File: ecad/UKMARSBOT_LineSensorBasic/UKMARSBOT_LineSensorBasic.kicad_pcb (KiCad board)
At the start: 2 copper layers, 40.5 x 81.4 mm, 32 parts, among them J1 Conn_01x16, Q1 BC337, Q2 BPW85C, Q3 BPW85C, Q4 BPW85C, Q5 BPW85C, Q6 BC337

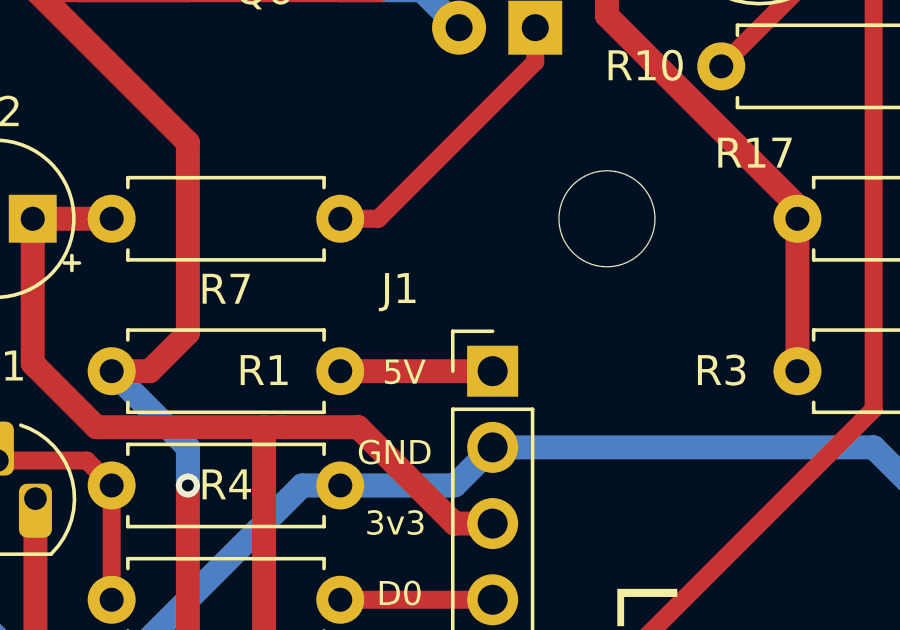
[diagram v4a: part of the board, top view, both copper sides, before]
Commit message: Reworked chassis board for production
Board reworked based on known issues from prototype builds.
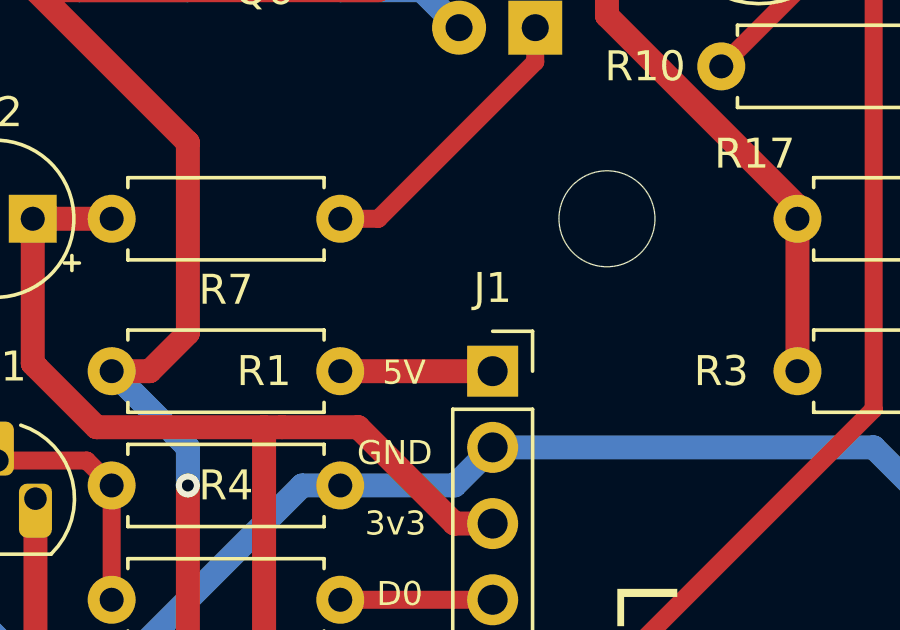
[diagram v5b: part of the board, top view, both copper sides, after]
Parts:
- J1: footprint Connector_PinHeader_2.54mm:PinHeader_1x16_P2.54mm_Vertical -> Connector_PinSocket_2.54mm:PinSocket_1x16_P2.54mm_Vertical
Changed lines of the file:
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@@
 		)
 	)
-	(footprint "Connector_PinHeader_2.54mm:PinHeader_1x16_P2.54mm_Vertical"
+	(footprint "Connector_PinSocket_2.54mm:PinSocket_1x16_P2.54mm_Vertical"
 		(locked yes)
 		(layer "F.Cu")
 		(at 157.48 82.55)
-		(descr "Through hole straight pin header, 1x16, 2.54mm pitch, single row")
-		(tags "Through hole pin header THT 1x16 2.54mm single row")
+		(descr "Through hole straight socket strip, 1x16, 2.54mm pitch, single row (from Kicad 4.0.7), script generated")
+		(tags "Through hole socket strip THT 1x16 2.54mm single row")
 		(property "Reference" "J1"
-			(at -3.084319 -2.733641 0)
+			(at 0 -2.77 0)
 			(layer "F.SilkS")
 			(effects
@@
 		)
 		(property "Value" "Conn_01x16"
-			(at 0 40.43 0)
+			(at 0 40.87 0)
 			(layer "F.Fab")
 			(effects
@@
 			)
 		)
-		(property "Footprint" "Connector_PinHeader_2.54mm:PinHeader_1x16_P2.54mm_Vertical"
+		(property "Footprint" "Connector_PinSocket_2.54mm:PinSocket_1x16_P2.54mm_Vertical"
 			(at 0 0 0)
 			(unlocked yes)
@@
 		(attr through_hole)
 		(fp_line
-			(start -1.33 -1.33)
-			(end 0 -1.33)
-			(stroke
-				(width 0.12)
-				(type solid)
-			)
-			(layer "F.SilkS")
-		)
-		(fp_line
-			(start -1.33 0)
-			(end -1.33 -1.33)
-			(stroke
-				(width 0.12)
-				(type solid)
-			)
-			(layer "F.SilkS")
-		)
-		(fp_line
 			(start -1.33 1.27)
 			(end -1.33 39.43)
@@
 		)
 		(fp_line
+			(start 0 -1.33)
+			(end 1.33 -1.33)
+			(stroke
+				(width 0.12)
+				(type solid)
+			)
+			(layer "F.SilkS")
+		)
+		(fp_line
+			(start 1.33 -1.33)
+			(end 1.33 0)
+			(stroke
+				(width 0.12)
+				(type solid)
+			)
+			(layer "F.SilkS")
+		)
+		(fp_line
 			(start 1.33 1.27)
 			(end 1.33 39.43)
@@
 		(fp_line
 			(start -1.8 -1.8)
+			(end 1.75 -1.8)
+			(stroke
+				(width 0.05)
+				(type solid)
+			)
+			(layer "F.CrtYd")
+		)
+		(fp_line
+			(start -1.8 39.9)
+			(end -1.8 -1.8)
+			(stroke
+				(width 0.05)
+				(type solid)
+			)
+			(layer "F.CrtYd")
+		)
+		(fp_line
+			(start 1.75 -1.8)
+			(end 1.75 39.9)
+			(stroke
+				(width 0.05)
+				(type solid)
+			)
+			(layer "F.CrtYd")
+		)
+		(fp_line
+			(start 1.75 39.9)
 			(end -1.8 39.9)
 			(stroke
@@
 		)
 		(fp_line
-			(start -1.8 39.9)
-			(end 1.8 39.9)
-			(stroke
-				(width 0.05)
-				(type solid)
-			)
-			(layer "F.CrtYd")
-		)
-		(fp_line
-			(start 1.8 -1.8)
-			(end -1.8 -1.8)
-			(stroke
-				(width 0.05)
-				(type solid)
-			)
-			(layer "F.CrtYd")
-		)
-		(fp_line
-			(start 1.8 39.9)
-			(end 1.8 -1.8)
-			(stroke
-				(width 0.05)
-				(type solid)
-			)
-			(layer "F.CrtYd")
-		)
-		(fp_line
-			(start -1.27 -0.635)
-			(end -0.635 -1.27)
+			(start -1.27 -1.27)
+			(end 0.635 -1.27)
 			(stroke
 				(width 0.1)
@@
 		(fp_line
 			(start -1.27 39.37)
-			(end -1.27 -0.635)
-			(stroke
-				(width 0.1)
-				(type solid)
-			)
-			(layer "F.Fab")
-		)
-		(fp_line
-			(start -0.635 -1.27)
-			(end 1.27 -1.27)
-			(stroke
-				(width 0.1)
-				(type solid)
-			)
-			(layer "F.Fab")
-		)
-		(fp_line
-			(start 1.27 -1.27)
+			(end -1.27 -1.27)
+			(stroke
+				(width 0.1)
+				(type solid)
+			)
+			(layer "F.Fab")
+		)
+		(fp_line
+			(start 0.635 -1.27)
+			(end 1.27 -0.635)
+			(stroke
+				(width 0.1)
+				(type solid)
+			)
+			(layer "F.Fab")
+		)
+		(fp_line
+			(start 1.27 -0.635)
 			(end 1.27 39.37)
 			(stroke
@@
 			(pintype "passive")
 		)
-		(model "${KICAD8_3DMODEL_DIR}/Connector_PinHeader_2.54mm.3dshapes/PinHeader_1x16_P2.54mm_Vertical.wrl"
+		(model "${KICAD8_3DMODEL_DIR}/Connector_PinSocket_2.54mm.3dshapes/PinSocket_1x16_P2.54mm_Vertical.wrl"
 			(offset
 				(xyz 0 0 0)

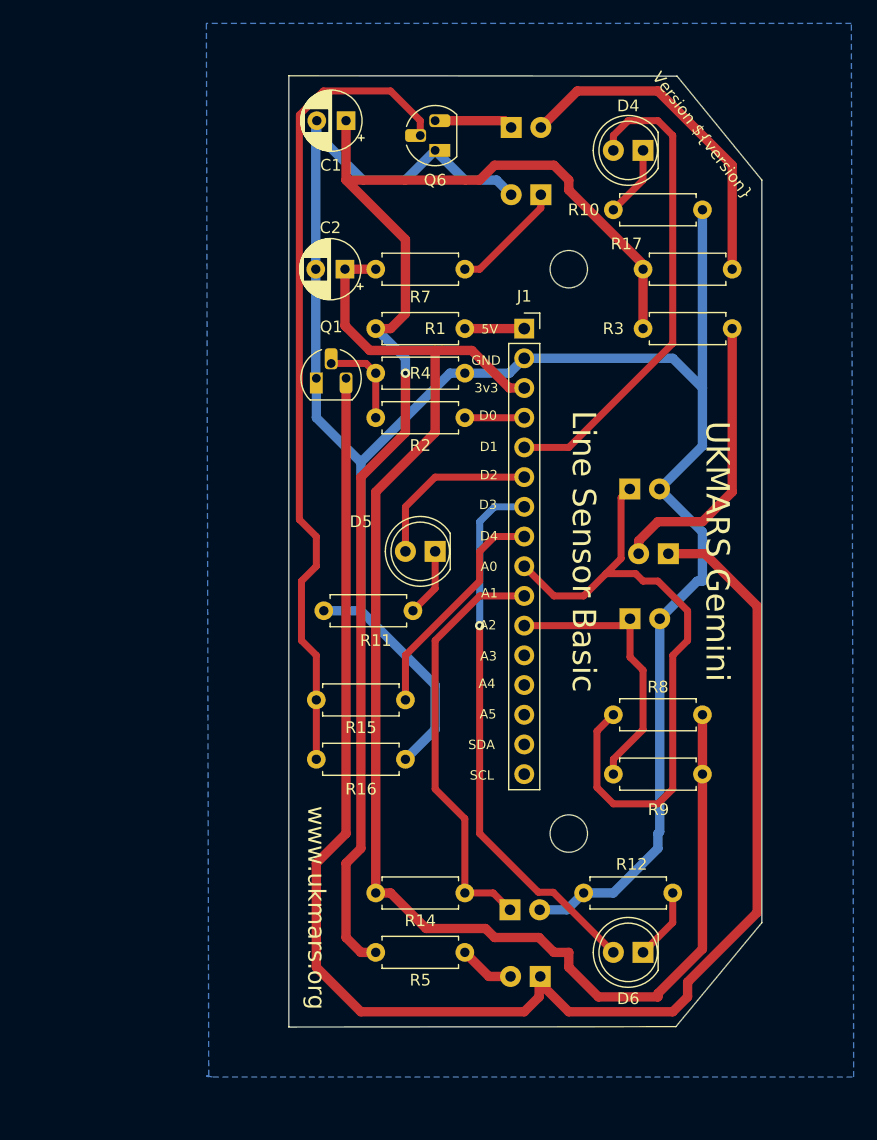
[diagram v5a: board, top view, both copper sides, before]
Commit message: Updated basic line follower board
Updated for v2.0 board set addressing all issues raised on the prototype board.
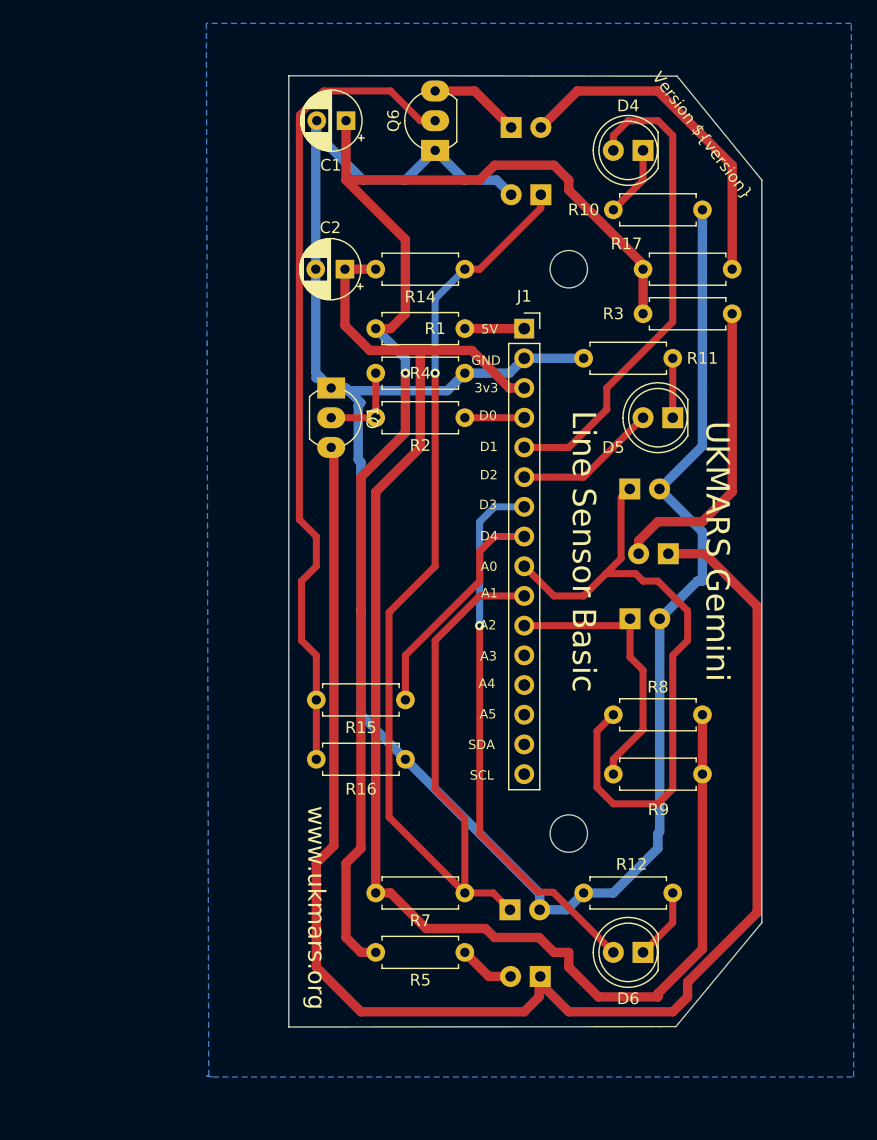
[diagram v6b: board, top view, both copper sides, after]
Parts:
- C2: value 10uF -> 100uF
- Q1, Q6: value BC337 -> BC337-40; footprint Package_TO_SOT_THT:TO-92_HandSolder -> ukmarsbot:BC337
- R14: renamed from R7; value 2K2 -> 680R
- R7: renamed from R14; value 2K2 -> 680R
- R8, R9: value 2K2 -> 680R
- moved R11 31.0 mm to (170.2, 85.1)
- moved D5 23.3 mm to (170.2, 90.2)
- moved Q1 1.52 mm to (141.0, 87.6), turned to -90 degrees
- moved R3 1.27 mm to (175.3, 81.3)
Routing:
- net SEN1AIP: track 46.1 -> 104.8 mm, vias 0 -> 1
- net Net-(D1-K): track 134.4 -> 128.2 mm
- net SEN2DI0: track 15.0 -> 12.3 mm
- net GND: track 190.8 -> 193.1 mm
- net Vemit: track 115.4 -> 114.1 mm
- net Net-(D1-A): track 24.8 -> 26.1 mm
- net Net-(D7-K): track 6.74 -> 7.79 mm
- net Net-(D5-K): track 5.86 -> 5.08 mm
- net 3v3: track 127.8 -> 127.2 mm

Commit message: Add v2 wall sensor board
Wall sensor updated for Issues raised on prototype builds. Better pin markings added to Line sensor, mezz and chassis boards
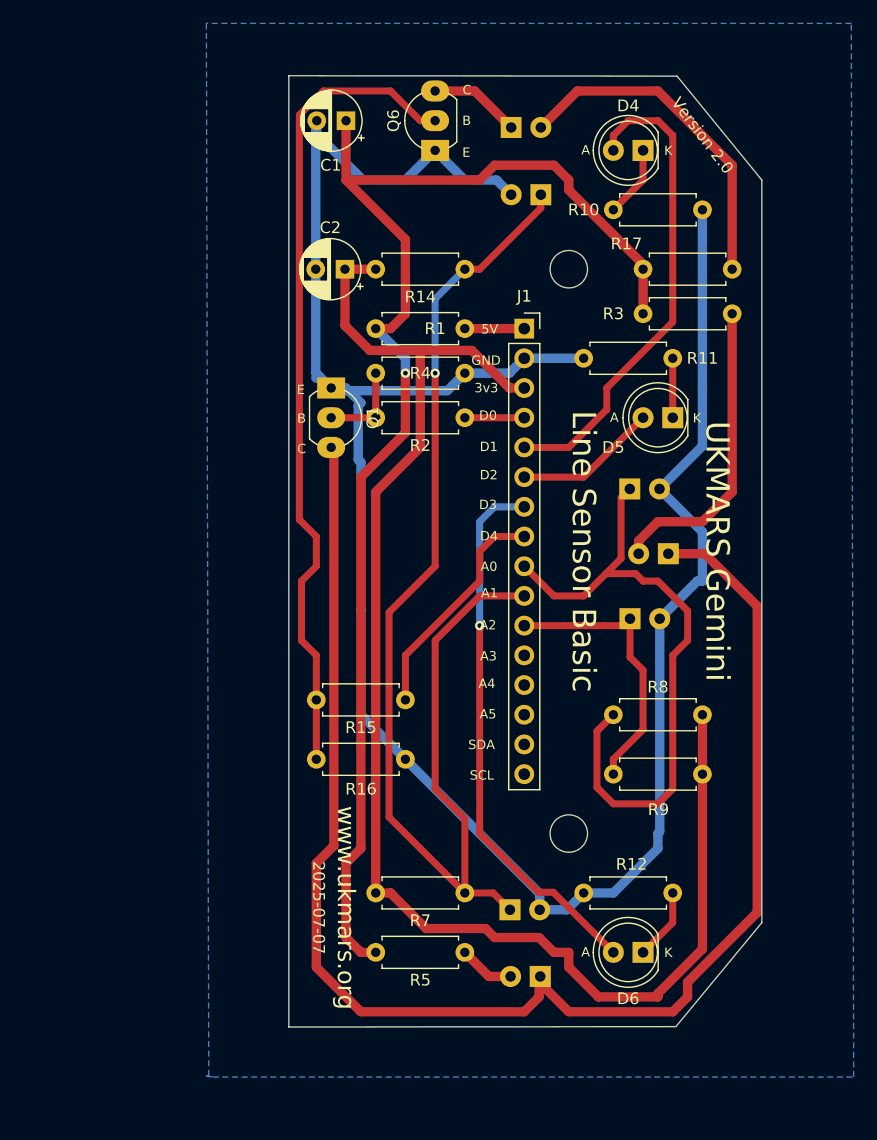
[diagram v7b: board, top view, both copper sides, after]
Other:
- board text added: "2025-07-07"
- board text added: "A"
- board text added: "B"
- board text added: "C"
- board text added: "E"
- board text added: "K"
- board text added: "Version 2.0"
- board text removed: "Version ${version}"
- board text removed: "Version 1.0"
